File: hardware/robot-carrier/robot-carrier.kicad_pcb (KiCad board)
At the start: 2 copper layers, 160 x 100 mm, 32 parts, among them J1 DC INPUT 6S 18-25.2V, J10 M1, J11 M2, J12 M3, J13 M4, J20 S1, J21 S2, J22 S3, J23 S4, J24 S5, J25 S6, J30 IMU / DISTANCE I2C, U6 Mornsun URF2405QB-100WR3 9-36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

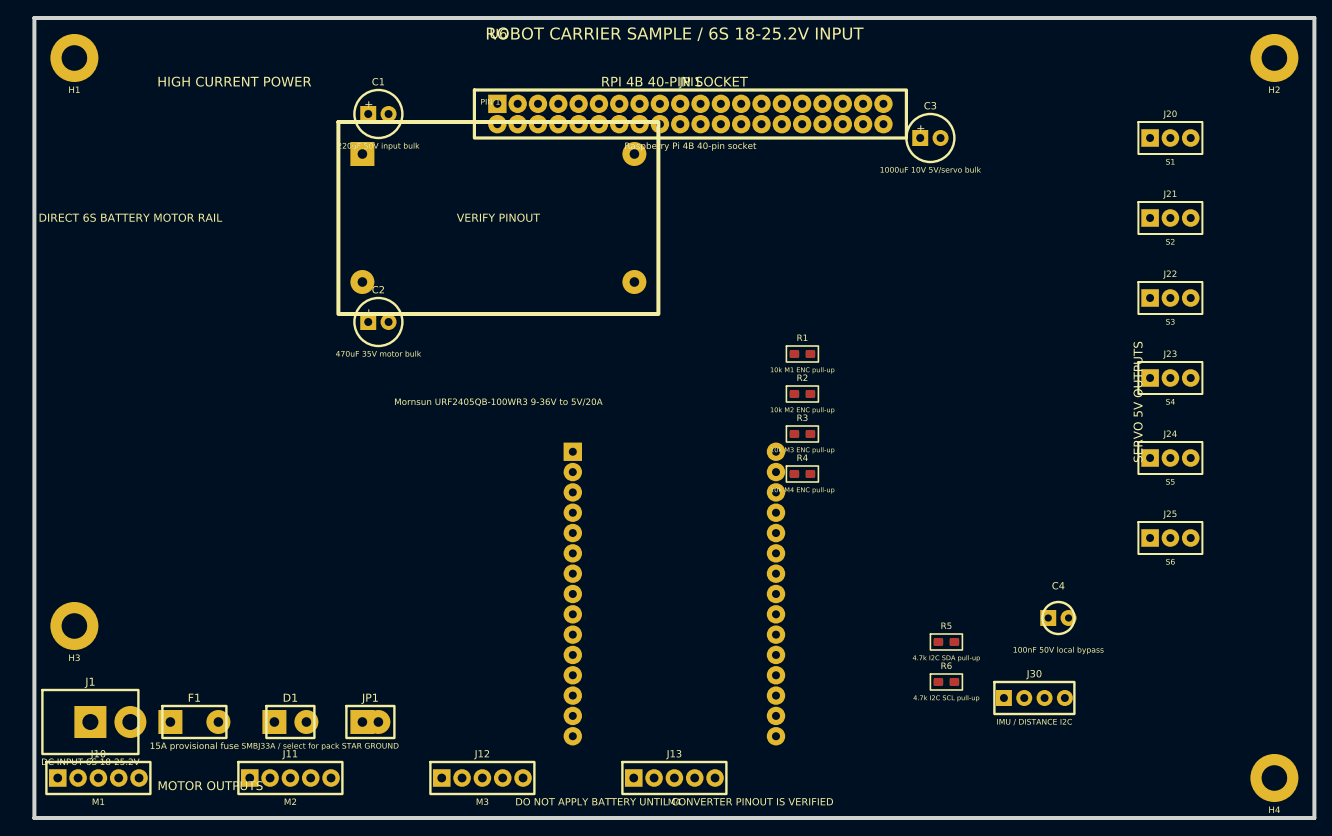
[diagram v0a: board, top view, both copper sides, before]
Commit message: Add compact ESP32 robot carrier placement
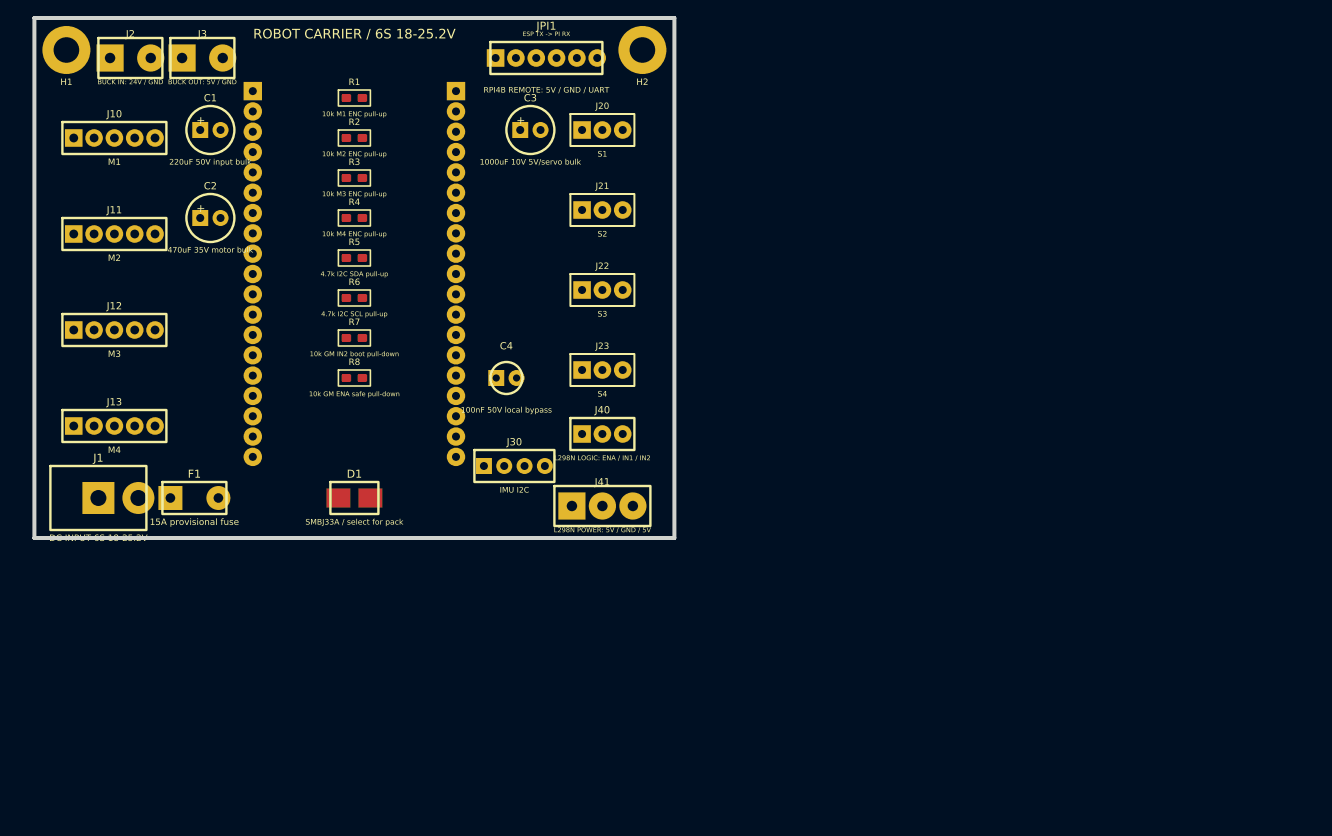
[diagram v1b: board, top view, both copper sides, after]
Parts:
- removed H3, H4: M3, Custom:MountingHole_M3
- removed J24: S5, Custom:SERVO_3PIN
- removed J25: S6, Custom:SERVO_3PIN
- removed JP1: STAR GROUND, Custom:POWER_LINK
- removed U6: Mornsun URF2405QB-100WR3 9-36V to 5V/20A, Custom:CONVERTER_1_4_BRICK
- added J2: BUCK IN: 24V / GND, Custom:TERM_BLOCK_1X02, F.Cu at (32.0, 25.0)
- added J3: BUCK OUT: 5V / GND, Custom:TERM_BLOCK_1X02, F.Cu at (41.0, 25.0)
- added J40: L298N LOGIC: ENA / IN1 / IN2, Custom:DUPONT_MALE_1X03, F.Cu at (91.0, 72.0)
- added J41: L298N POWER: 5V / GND / 5V, Custom:TERM_BLOCK_1X03, F.Cu at (91.0, 81.0)
- added R7: 10k GM IN2 boot pull-down, Custom:R_0805, F.Cu at (60.0, 60.0)
- added R8: 10k GM ENA safe pull-down, Custom:R_0805, F.Cu at (60.0, 65.0)
- J30: value IMU / DISTANCE I2C -> IMU I2C
- JESP1: value ESP32-WROOM-32 DevKit 30-pin socket -> 2x Dupont female 1x19, 38-pin ESP32 DevKitC; footprint Custom:ESP32_30PIN_SOCKET -> Custom:ESP32_DEVKITC_38PIN_SOCKET
- JPI1: value Raspberry Pi 4B 40-pin socket -> RPI4B REMOTE: 5V / GND / UART; footprint Custom:PI4B_40PIN -> Custom:PI_REMOTE_1X06_MALE
- moved R5 88.2 mm to (60.0, 50.0)
- moved R6 88.2 mm to (60.0, 55.0)
- moved J13 82.7 mm to (30.0, 71.0)
- moved J10 80.0 mm to (30.0, 35.0)
- moved H2 79.0 mm to (96.0, 24.0)
- moved C4 75.2 mm to (79.0, 65.0)
- moved J12 72.5 mm to (30.0, 59.0)
- moved J11 71.5 mm to (30.0, 47.0)
- moved J30 71.2 mm to (80.0, 76.0)
- moved J20 71.0 mm to (91.0, 34.0)
- moved J21 71.0 mm to (91.0, 44.0)
- moved J22 71.0 mm to (91.0, 54.0)
- moved J23 71.0 mm to (91.0, 64.0)
- moved R1 64.5 mm to (60.0, 30.0)
- moved R2 64.5 mm to (60.0, 35.0)
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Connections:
- J30 pad 1: +5V -> +3V3
- JESP1 pad 13: (no net) -> GM_IN2_3V3
- JESP1 pad 16: +5V -> (no net)
- JESP1 pad 17: GND -> (no net)
- JESP1 pad 18: M1_DIR_3V3 -> (no net)
- JESP1 pad 19: S5_PWM -> +5V
- JESP1 pad 20: (no net) -> GND
- JESP1 pad 21: (no net) -> M1_DIR_3V3
- JESP1 pad 22: S4_PWM -> GM_ENA_PWM_3V3
- JESP1 pad 23: S3_PWM -> PI_UART_TX_3V3
- JESP1 pad 24: M4_PWM_3V3 -> PI_UART_RX_3V3
- JESP1 pad 25: I2C_SDA -> S4_PWM
- JESP1 pad 26: M3_PWM_3V3 -> GND
- JESP1 pad 27: M2_PWM_3V3 -> S3_PWM
- JESP1 pad 28: S1_PWM -> M4_PWM_3V3
- JESP1 pad 29: (no net) -> I2C_SDA
- JESP1 pad 30: (no net) -> M3_PWM_3V3
- JESP1 pad 7: S6_PWM -> GM_IN1_3V3
- JPI1 pad 1: (no net) -> +5V
- JPI1 pad 3: I2C_SDA -> GND
- JPI1 pad 4: +5V -> GND
- JPI1 pad 5: I2C_SCL -> PI_UART_TX_3V3
- JPI1 pad 6: GND -> PI_UART_RX_3V3
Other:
- board size 160 x 100 mm -> 80 x 65 mm
- board text added: "ROBOT CARRIER / 6S 18-25.2V"
- board text removed: "DIRECT 6S BATTERY MOTOR RAIL"
- board text removed: "DO NOT APPLY BATTERY UNTIL CONVERTER PINOUT IS VERIFIED"
- board text removed: "HIGH CURRENT POWER"
- board text removed: "MOTOR OUTPUTS"
- board text removed: "ROBOT CARRIER SAMPLE / 6S 18-25.2V INPUT"
- board text removed: "RPI 4B 40-PIN SOCKET"
- board text removed: "SERVO 5V OUTPUTS"

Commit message: Refine carrier input and IMU interface
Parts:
- C1: value 220uF 50V input bulk -> 220uF 50V, LCSC C44705; footprint Custom:RADIAL_CAP -> Capacitor_THT:CP_Radial_D10.0mm_P5.00mm
- C2: value 470uF 35V motor bulk -> 470uF 35V, LCSC C46551024; footprint Custom:RADIAL_CAP -> Capacitor_THT:CP_Radial_D8.0mm_P3.50mm
- C3: value 1000uF 10V 5V/servo bulk -> 1000uF 10V, LCSC C79119; footprint Custom:RADIAL_CAP -> Capacitor_THT:CP_Radial_D8.0mm_P3.50mm
- C4: value 100nF 50V local bypass -> 100nF 50V, LCSC C502153; footprint Custom:RADIAL_CAP -> Capacitor_SMD:C_0805_2012Metric
- D1: value SMBJ33A / select for pack -> SMBJ33A, LCSC C78419; footprint Custom:TVS_DIODE -> Diode_SMD:D_SMB
- J2: value BUCK IN: 24V / GND -> DB128L 2P, LCSC C500021
- J3: value BUCK OUT: 5V / GND -> DB128L 2P, LCSC C500021
- J30: value IMU I2C -> WT901 I2C
- J41: value L298N POWER: 5V / GND / 5V -> DB128L 3P, LCSC C430602

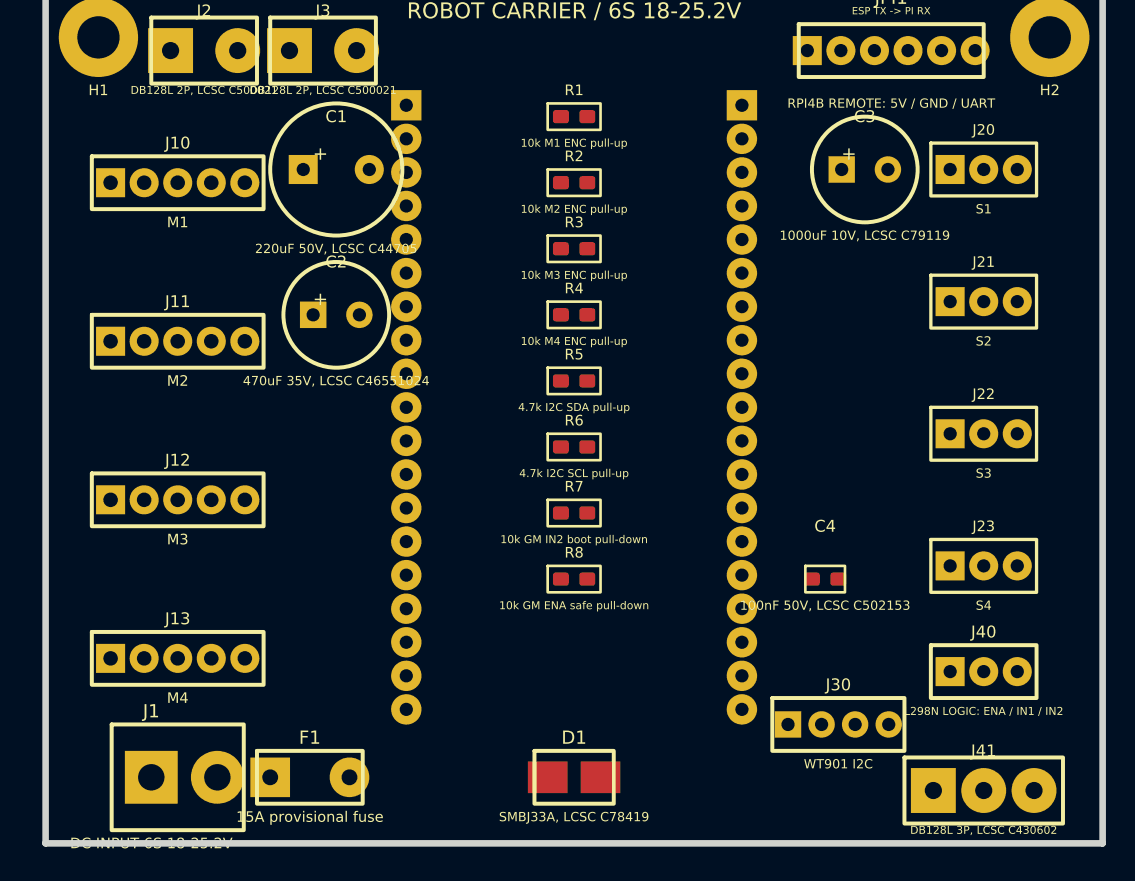
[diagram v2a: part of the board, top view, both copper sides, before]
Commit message: Add authoritative carrier schematic and hand-solder layout
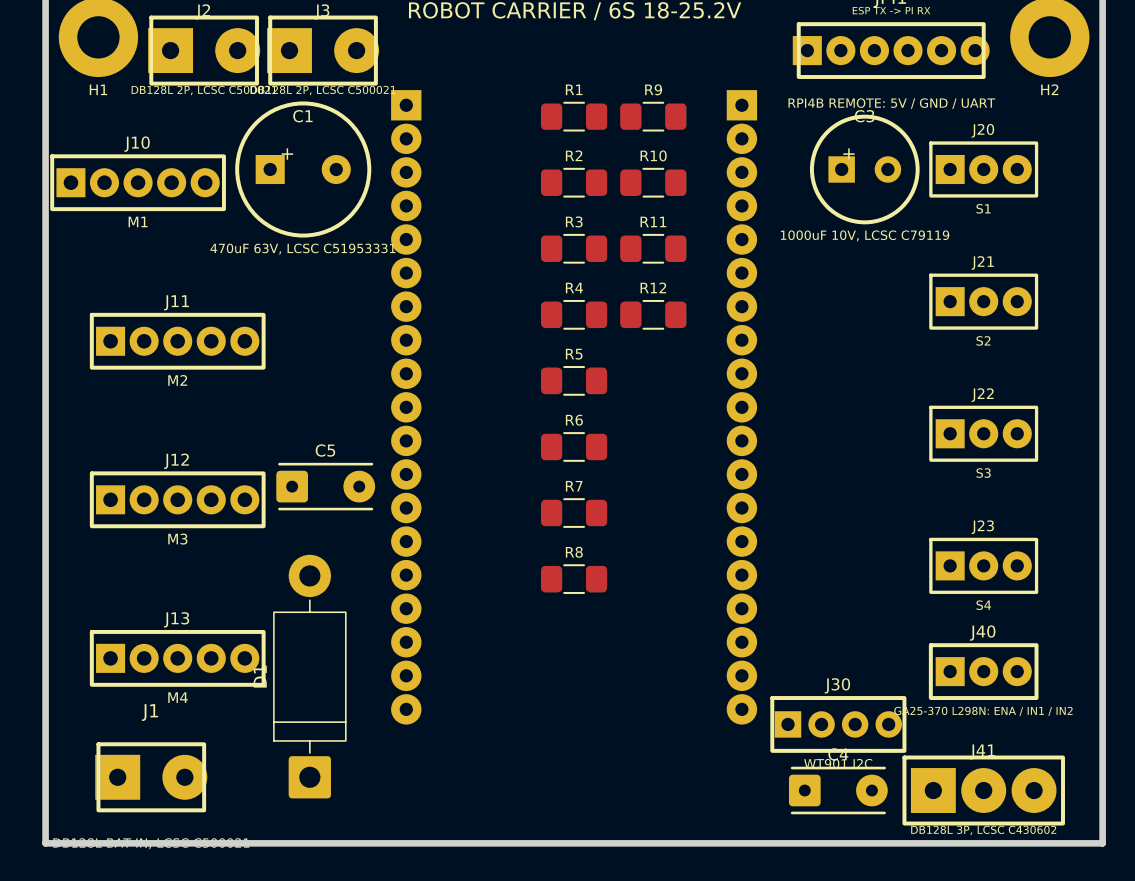
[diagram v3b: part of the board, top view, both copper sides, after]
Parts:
- removed C2: 470uF 35V, LCSC C46551024, Capacitor_THT:CP_Radial_D8.0mm_P3.50mm
- removed F1: 15A provisional fuse, Custom:FUSE_5A
- added C5: 100nF 50V 24V shared, LCSC C84772, Custom:C_THT_P5.08_HAND, F.Cu at (41.2, 58.0)
- added R10: 10k M2 PWM safe pull-up, Custom:R_1206_HAND, F.Cu at (66.0, 35.0)
- added R11: 10k M3 PWM safe pull-up, Custom:R_1206_HAND, F.Cu at (66.0, 40.0)
- added R12: 10k M4 PWM safe pull-up, Custom:R_1206_HAND, F.Cu at (66.0, 45.0)
- added R9: 10k M1 PWM safe pull-up, Custom:R_1206_HAND, F.Cu at (66.0, 30.0)
- C1: value 220uF 50V, LCSC C44705 -> 470uF 63V, LCSC C51953331
- C4: value 100nF 50V, LCSC C502153 -> 100nF 50V 5V shared, LCSC C84772; footprint Capacitor_SMD:C_0805_2012Metric -> Custom:C_THT_P5.08_HAND
- D1: value SMBJ33A, LCSC C78419 -> 1.5KE33A, LCSC C18198472; footprint Diode_SMD:D_SMB -> Diode_THT:D_DO-201AD_P15.24mm_Horizontal
- J1: value DC INPUT 6S 18-25.2V -> DB128L BAT IN, LCSC C500021; footprint Custom:DC_Barrel_5.5mm -> Custom:TERM_BLOCK_1X02
- J40: value L298N LOGIC: ENA / IN1 / IN2 -> GA25-370 L298N: ENA / IN1 / IN2
- R1, R2, R3, R4, R5, R6: footprint Custom:R_0805 -> Custom:R_1206_HAND
- R7: value 10k GM IN2 boot pull-down -> 10k GA25 IN2 boot pull-down; footprint Custom:R_0805 -> Custom:R_1206_HAND
- R8: value 10k GM ENA safe pull-down -> 10k GA25 ENA safe pull-down; footprint Custom:R_0805 -> Custom:R_1206_HAND
- moved D1 20.0 mm to (40.0, 80.0), turned to 90 degrees
- moved C4 16.0 mm to (80.0, 81.0)
- moved J10 3.00 mm to (27.0, 35.0)
- moved C1 2.50 mm to (39.5, 34.0)
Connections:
- net GM_ENA_PWM_3V3 renamed GA25_ENA_PWM_3V3
- net GM_IN1_3V3 renamed GA25_IN1_3V3
- net GM_IN2_3V3 renamed GA25_IN2_3V3
- J1 pad 1: VIN_BAT -> VIN_PROTECTED

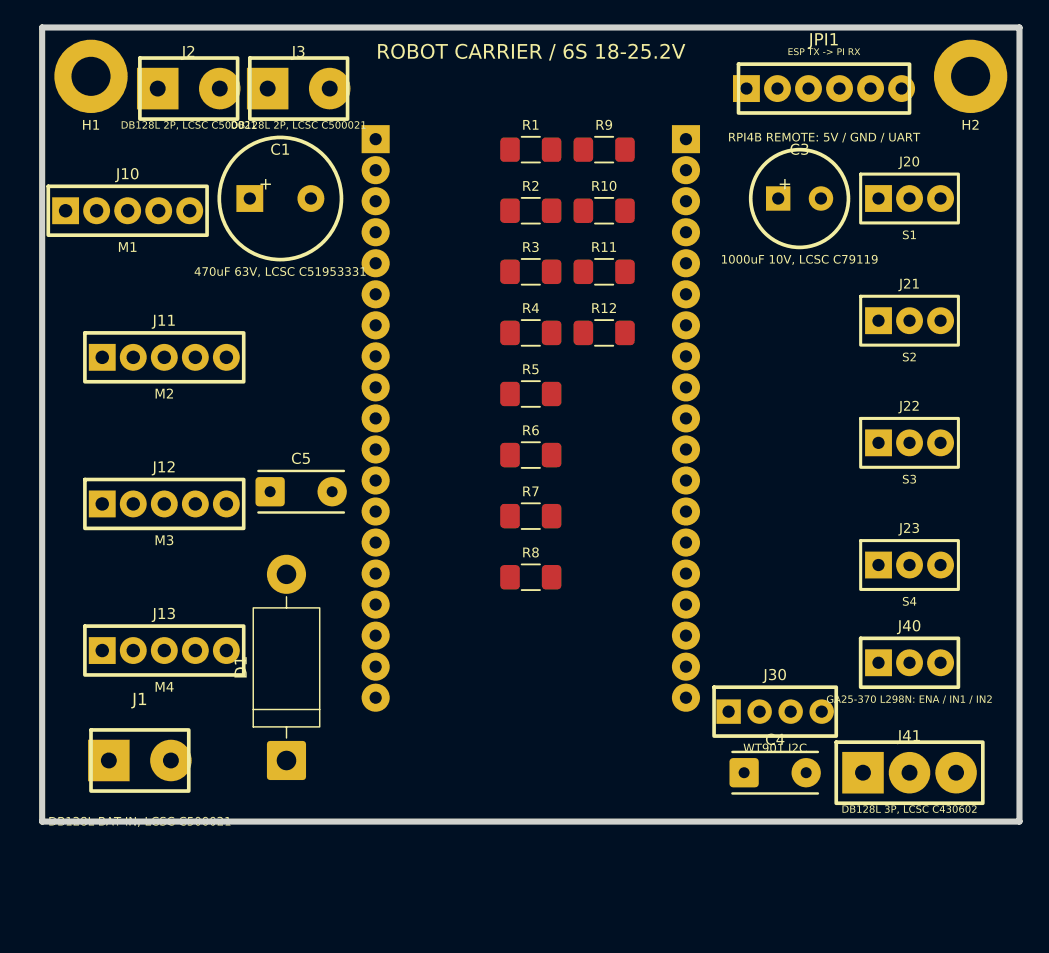
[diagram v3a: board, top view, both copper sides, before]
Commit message: Checkpoint autorouted carrier layout
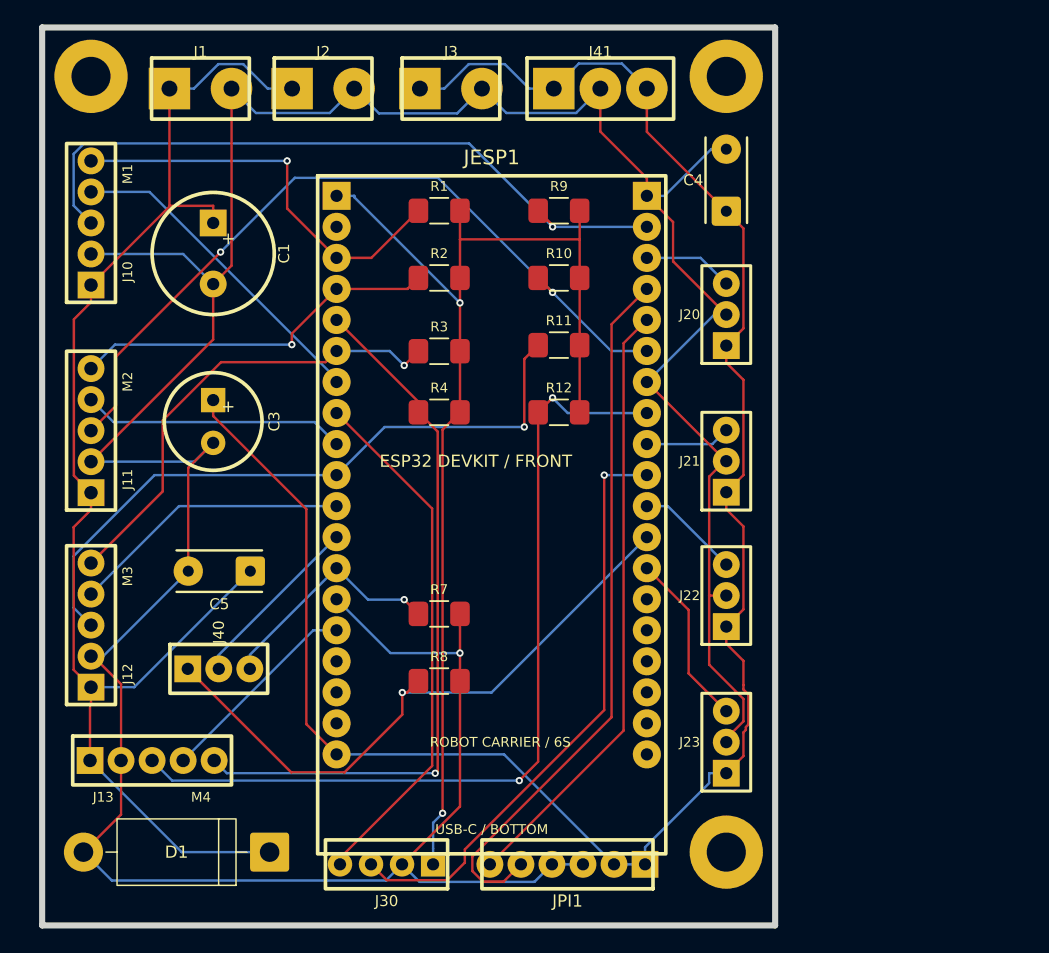
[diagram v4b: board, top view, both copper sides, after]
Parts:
- removed R5: 4.7k I2C SDA pull-up, Custom:R_1206_HAND
- removed R6: 4.7k I2C SCL pull-up, Custom:R_1206_HAND
- added H3: M3, Custom:MountingHole_M3, F.Cu at (76.0, 87.5)
- J30: value WT901 I2C -> WT901 UART; footprint Custom:I2C_1X04 -> Custom:UART_1X04
- JESP1: moved to F.Cu
- moved JPI1 66.9 mm to (63.0, 88.5), turned to 180 degrees
- moved J41 61.5 mm to (65.7, 25.0)
- moved J40 56.5 mm to (34.5, 72.5)
- moved J1 55.2 mm to (33.0, 25.0)
- moved C3 51.4 mm to (34.0, 52.2), turned to -90 degrees
- moved C4 48.7 mm to (76.0, 32.5), turned to 90 degrees
- moved J30 34.2 mm to (48.2, 88.5), turned to 180 degrees
- moved J23 20.9 mm to (76.0, 78.5), turned to 90 degrees
- moved H2 20.0 mm to (76.0, 24.0)
- moved J22 19.5 mm to (76.0, 66.5), turned to 90 degrees
- moved J21 18.9 mm to (76.0, 55.5), turned to 90 degrees
- moved J20 17.8 mm to (76.0, 43.5), turned to 90 degrees
- moved J3 12.5 mm to (53.5, 25.0)
- moved J12 11.6 mm to (24.0, 68.9), turned to 90 degrees
- moved R8 11.3 mm to (52.5, 73.5)
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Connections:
- net I2C_SCL renamed IMU_UART_RX_3V3
- net I2C_SDA renamed IMU_UART_TX_3V3
- JESP1 pad 10: M3_DIR_3V3 -> M3_PWM_3V3
- JESP1 pad 11: M4_DIR_3V3 -> M3_DIR_3V3
- JESP1 pad 12: S2_PWM -> GA25_IN1_3V3
- JESP1 pad 15: M1_PWM_3V3 -> M4_DIR_3V3
- JESP1 pad 21: M1_DIR_3V3 -> M1_PWM_3V3
- JESP1 pad 22: GA25_ENA_PWM_3V3 -> S1_PWM
- JESP1 pad 25: S4_PWM -> M2_PWM_3V3
- JESP1 pad 27: S3_PWM -> M4_PWM_3V3
- JESP1 pad 28: M4_PWM_3V3 -> S2_PWM
- JESP1 pad 3: M3_ENC -> M1_ENC
- JESP1 pad 30: M3_PWM_3V3 -> S3_PWM
- JESP1 pad 31: M2_PWM_3V3 -> GA25_ENA_PWM_3V3
- JESP1 pad 32: S1_PWM -> S4_PWM
- JESP1 pad 4: M4_ENC -> M2_ENC
- JESP1 pad 5: M1_ENC -> M4_ENC
- JESP1 pad 6: M2_ENC -> M3_ENC
- JESP1 pad 7: GA25_IN1_3V3 -> M1_DIR_3V3
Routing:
- net GND: track 0.00 -> 286.3 mm, vias 0 -> 1
- net +5V: track 0.00 -> 158.8 mm
- net VIN_PROTECTED: track 0.00 -> 111.5 mm
- net +3V3: track 0.00 -> 94.5 mm, vias 0 -> 2
- net M4_PWM_3V3: track 0.00 -> 71.4 mm, vias 0 -> 2
- net M2_PWM_3V3: track 0.00 -> 64.0 mm, vias 0 -> 2
- net M4_ENC: track 0.00 -> 59.1 mm, vias 0 -> 1
- net PI_UART_TX_3V3: track 0.00 -> 58.5 mm
- net M1_PWM_3V3: track 0.00 -> 58.2 mm, vias 0 -> 1
- net M3_PWM_3V3: track 0.00 -> 54.7 mm, vias 0 -> 1
- net GA25_ENA_PWM_3V3: track 0.00 -> 51.8 mm, vias 0 -> 1
- net PI_UART_RX_3V3: track 0.00 -> 49.9 mm
- net IMU_UART_TX_3V3: track 0.00 -> 48.8 mm, vias 0 -> 1
- net IMU_UART_RX_3V3: track 0.00 -> 43.3 mm
- net M3_ENC: track 0.00 -> 38.4 mm, vias 0 -> 1
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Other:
- board size 80 x 65 mm -> 60 x 73.5 mm
- board text added: "ESP32 DEVKIT / FRONT"
- board text added: "ROBOT CARRIER / 6S"
- board text removed: "ESP32 DEVKIT / UNDERSIDE"
- board text removed: "ROBOT CARRIER / 6S 18-25.2V"
